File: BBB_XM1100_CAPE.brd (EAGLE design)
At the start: 54.6 x 71.8 mm, 24 parts, among them U2 MIC5225-3.3

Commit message: BOM updates associated with populating first test boards
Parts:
- C4: value 1uF -> 47pF
- L1: value 33NH -> 39NH
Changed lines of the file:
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@@
 <attribute name="NAME" x="41.021" y="20.955" size="1.27" layer="25" ratio="10" rot="R90"/>
 </element>
-<element name="C4" library="rcl" package="C0805" value="1uF" x="16.51" y="11.43" smashed="yes" rot="R180">
+<element name="C4" library="rcl" package="C0805" value="47pF" x="16.51" y="11.43" smashed="yes" rot="R180">
 <attribute name="NAME" x="16.764" y="12.954" size="0.508" layer="25" rot="R180"/>
 </element>
-<element name="L1" library="SparkFun-Coils" package="0402" value="33NH" x="20.066" y="11.176" smashed="yes" rot="R180">
+<element name="L1" library="SparkFun-Coils" package="0402" value="39NH" x="20.066" y="11.176" smashed="yes" rot="R180">
 <attribute name="NAME" x="20.447" y="12.446" size="0.508" layer="25" rot="R180"/>
 <attribute name="PROD_ID" value="NDUC-13457" x="20.066" y="11.176" size="1.778" layer="27" rot="R180" display="off"/>

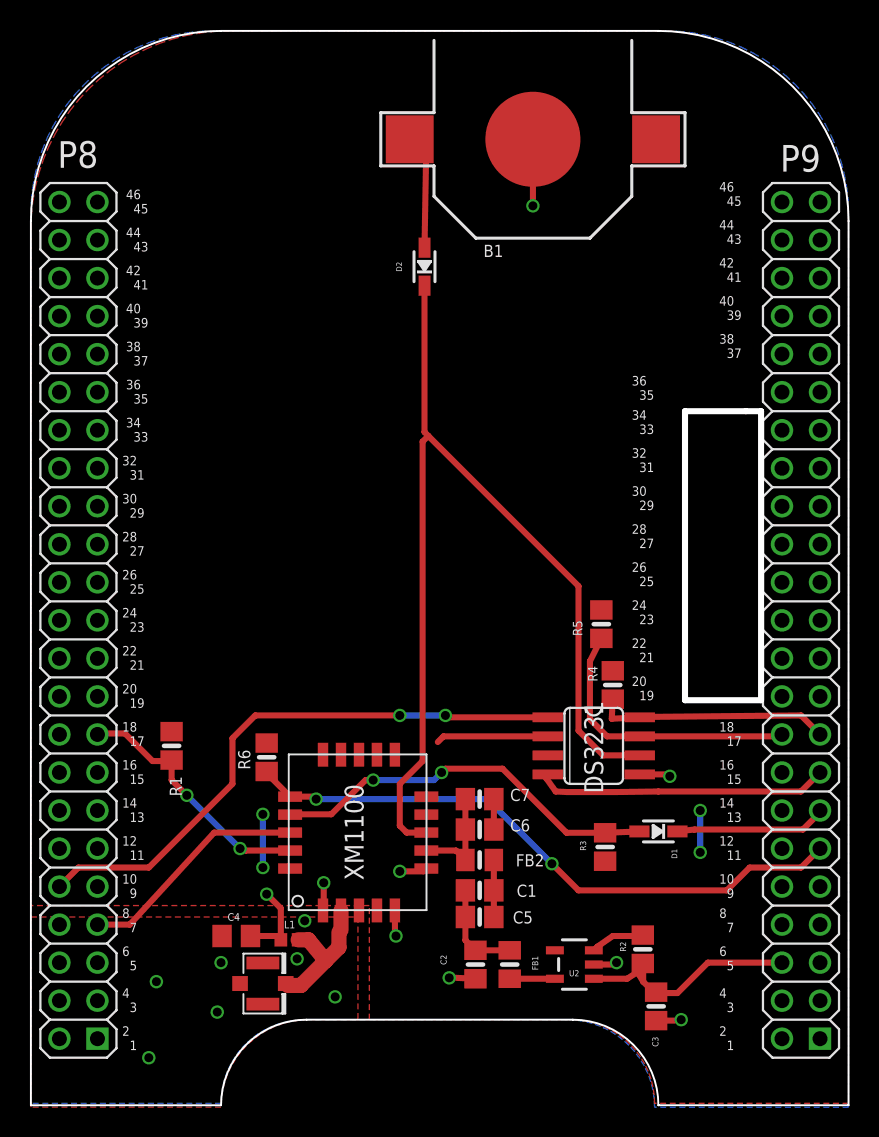
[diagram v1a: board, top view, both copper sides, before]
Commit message: minor updates to silkscreen layout to better match OSH Park silkscreen resolution
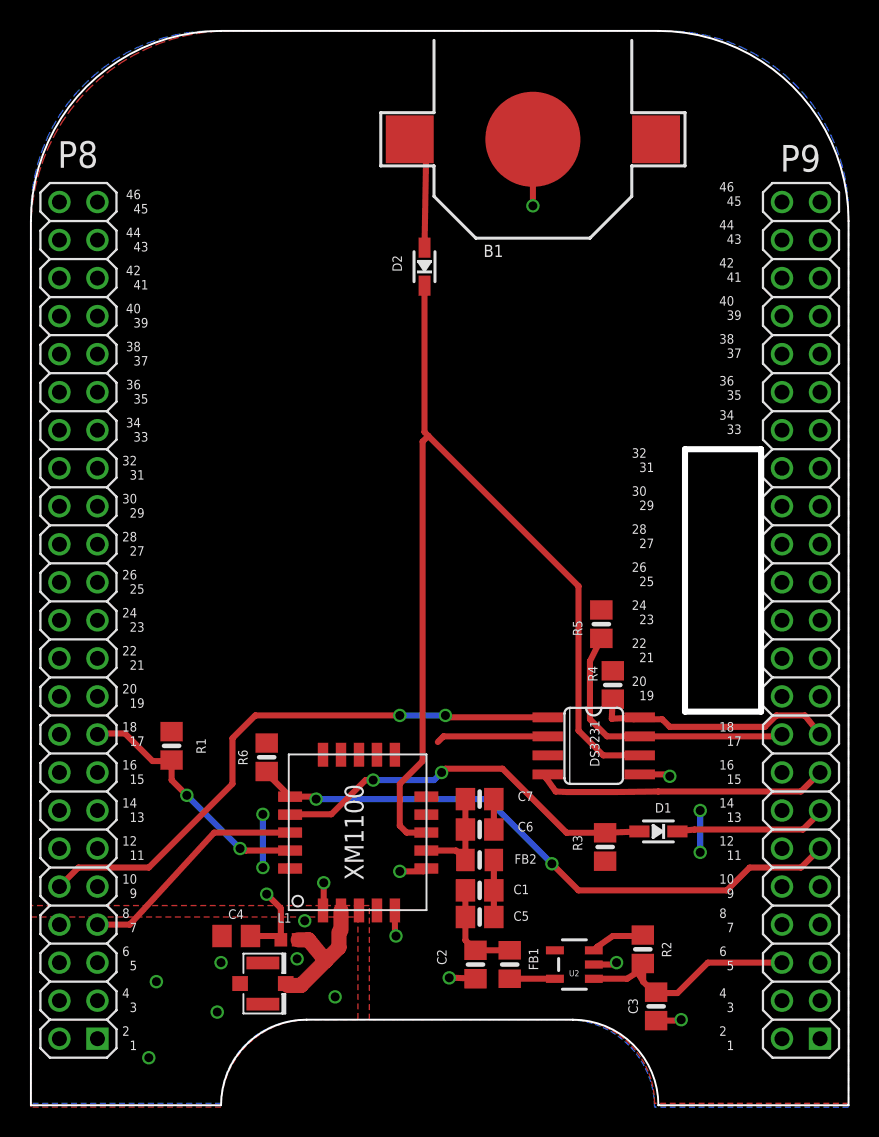
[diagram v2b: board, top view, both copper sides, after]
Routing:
- net SCL: track 15.7 -> 17.2 mm
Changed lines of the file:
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@@
 <text x="4.572" y="62.738" size="1.778" layer="25">P8</text>
 <polygon width="0.4064" layer="20">
-<vertex x="50.546" y="46.482"/>
-<vertex x="46.482" y="46.482"/>
-<vertex x="46.482" y="27.178"/>
-<vertex x="51.562" y="27.178"/>
-<vertex x="51.562" y="46.482"/>
+<vertex x="51.562" y="43.942"/>
+<vertex x="46.482" y="43.942"/>
+<vertex x="46.482" y="26.416"/>
+<vertex x="51.562" y="26.416"/>
 </polygon>
 <text x="8.89" y="3.81" size="0.635" layer="25">2
@@
 <text x="48.768" y="50.038" size="0.635" layer="25">38
   37</text>
-<text x="42.926" y="47.244" size="0.635" layer="25">36
+<text x="48.768" y="47.244" size="0.635" layer="25">36
   35</text>
-<text x="42.926" y="44.958" size="0.635" layer="25">34
+<text x="48.768" y="44.958" size="0.635" layer="25">34
   33</text>
 <text x="42.926" y="42.418" size="0.635" layer="25">32
@@
 </element>
 <element name="R2" library="microbuilder" package="0805-NO" value="10K" x="43.664" y="10.541" smashed="yes" rot="R270">
-<attribute name="NAME" x="42.14" y="11.049" size="0.4064" layer="25" ratio="15" rot="R270"/>
+<attribute name="NAME" x="44.934" y="11.049" size="0.635" layer="25" rot="R270"/>
 </element>
 <element name="C2" library="microbuilder" package="0805-NO" value="10uF" x="32.488" y="9.525" smashed="yes" rot="R270">
-<attribute name="NAME" x="30.559" y="9.501" size="0.4064" layer="25" ratio="15" rot="R90"/>
+<attribute name="NAME" x="30.559" y="9.501" size="0.635" layer="25" rot="R90"/>
 </element>
 <element name="FB1" library="microbuilder" package="0805-NO@1" value="Ferrite" x="34.774" y="9.525" smashed="yes" rot="R90">
-<attribute name="NAME" x="36.679" y="9.144" size="0.4064" layer="25" ratio="15" rot="R90"/>
+<attribute name="NAME" x="36.679" y="9.144" size="0.635" layer="25" rot="R90"/>
 </element>
 <element name="C3" library="microbuilder" package="0805-NO" value="10uF" x="44.553" y="6.731" smashed="yes" rot="R270">
-<attribute name="NAME" x="44.299" y="4.699" size="0.4064" layer="25" ratio="15" rot="R270"/>
+<attribute name="NAME" x="43.331" y="6.223" size="0.635" layer="25" rot="R90"/>
 </element>
 <element name="D1" library="microbuilder" package="SOD-323" value="1N4148" x="44.704" y="18.415" smashed="yes" rot="R180">
-<attribute name="NAME" x="45.582" y="17.25" size="0.381" layer="25" font="vector" ratio="15" rot="R270"/>
+<attribute name="NAME" x="44.472" y="19.674" size="0.635" layer="25" font="vector"/>
 </element>
 <element name="R3" library="microbuilder" package="0805-NO" value="10K" x="41.148" y="17.375" smashed="yes" rot="R90">
-<attribute name="NAME" x="39.878" y="17.121" size="0.4064" layer="25" ratio="15" rot="R90"/>
-</element>
-<element name="B1" library="microbuilder" package="CR1220" value="CR1220" x="36.322" y="64.643"/>
+<attribute name="NAME" x="39.624" y="17.121" size="0.635" layer="25" rot="R90"/>
+</element>
+<element name="B1" library="microbuilder" package="CR1220" value="CR1220" x="36.322" y="64.643" smashed="yes">
+<attribute name="NAME" x="33.02" y="56.783" size="0.8128" layer="25" font="vector" ratio="18"/>
+<attribute name="VALUE" x="33.02" y="55.775" size="0.635" layer="27" font="vector"/>
+</element>
 <element name="U$20" library="microbuilder" package="U.FL" value="U.FL" x="18.288" y="8.255" smashed="yes"/>
 <element name="D2" library="microbuilder" package="SOD-323" value="CUS520" x="29.083" y="56.134" smashed="yes" rot="R90">
-<attribute name="NAME" x="27.575" y="55.796" size="0.381" layer="25" ratio="18" rot="R90"/>
+<attribute name="NAME" x="27.575" y="55.796" size="0.635" layer="25" rot="R90"/>
 </element>
 <element name="U$15" library="adafruit" package="BEAGLEBONE_SHIELD" value="BEAGLEBONE_OUTLINE" x="2.794" y="-14.478" smashed="yes"/>
 <element name="R4" library="microbuilder" package="0805-NO" value="10K" x="41.656" y="28.194" smashed="yes" rot="R270">
-<attribute name="NAME" x="40.005" y="29.464" size="0.635" layer="25" ratio="18" rot="R270"/>
+<attribute name="NAME" x="40.005" y="29.464" size="0.635" layer="25" rot="R270"/>
 </element>
 <element name="R5" library="microbuilder" package="0805-NO" value="10K" x="40.894" y="32.258" smashed="yes" rot="R270">
-<attribute name="NAME" x="38.989" y="32.512" size="0.635" layer="25" ratio="18" rot="R270"/>
+<attribute name="NAME" x="38.989" y="32.512" size="0.635" layer="25" rot="R270"/>
 </element>
 <element name="DS3231" library="tuckerLib" package="SO08" value="DS3231M-8PIN" x="40.386" y="24.13" smashed="yes" rot="R270">
-<attribute name="NAME" x="41.021" y="20.955" size="1.27" layer="25" ratio="10" rot="R90"/>
+<attribute name="NAME" x="40.767" y="22.733" size="0.635" layer="25" rot="R90"/>
 </element>
 <element name="C4" library="rcl" package="C0805" value="47pF" x="16.51" y="11.43" smashed="yes" rot="R180">
-<attribute name="NAME" x="16.764" y="12.954" size="0.508" layer="25" rot="R180"/>
+<attribute name="NAME" x="17.018" y="13.208" size="0.635" layer="25" rot="R180"/>
 </element>
 <element name="L1" library="SparkFun-Coils" package="0402" value="39NH" x="20.066" y="11.176" smashed="yes" rot="R180">
-<attribute name="NAME" x="20.447" y="12.446" size="0.508" layer="25" rot="R180"/>
+<attribute name="NAME" x="20.193" y="12.954" size="0.635" layer="25" rot="R180"/>
 <attribute name="PROD_ID" value="NDUC-13457" x="20.066" y="11.176" size="1.778" layer="27" rot="R180" display="off"/>
 <attribute name="VALUE" value="3.9NH" x="20.066" y="11.176" size="1.778" layer="27" rot="R180" display="off"/>
@@
 <element name="U$3" library="tuckerLib" package="XM1100" value="XM1100" x="26.416" y="19.558" smashed="yes" rot="R90"/>
 <element name="FB2" library="microbuilder" package="0805-NO@1" value="Ferrite" x="32.766" y="16.51" smashed="yes" rot="R180">
-<attribute name="NAME" x="37.084" y="16.891" size="0.8128" layer="25" ratio="18" rot="R180"/>
+<attribute name="NAME" x="36.576" y="16.891" size="0.635" layer="25" rot="R180"/>
 </element>
 <element name="C1" library="microbuilder" package="0805-NO" value="1.0uF" x="32.766" y="14.478" smashed="yes" rot="R180">
-<attribute name="NAME" x="36.576" y="14.859" size="0.8128" layer="25" ratio="18" rot="R180"/>
+<attribute name="NAME" x="36.068" y="14.859" size="0.635" layer="25" rot="R180"/>
 </element>
 <element name="C5" library="microbuilder" package="0805-NO" value="0.1uF" x="32.766" y="12.7" smashed="yes" rot="R180">
-<attribute name="NAME" x="36.322" y="13.081" size="0.8128" layer="25" ratio="18" rot="R180"/>
+<attribute name="NAME" x="36.068" y="13.081" size="0.635" layer="25" rot="R180"/>
 </element>
 <element name="C6" library="microbuilder" package="0805-NO" value="1.0uF" x="32.766" y="18.542" smashed="yes">
-<attribute name="NAME" x="34.798" y="18.415" size="0.8128" layer="25" ratio="18"/>
+<attribute name="NAME" x="35.306" y="18.415" size="0.635" layer="25"/>
 </element>
 <element name="C7" library="microbuilder" package="0805-NO" value="0.1uF" x="32.766" y="20.574" smashed="yes">
-<attribute name="NAME" x="34.798" y="20.447" size="0.8128" layer="25" ratio="18"/>
+<attribute name="NAME" x="35.306" y="20.447" size="0.635" layer="25"/>
 </element>
 <element name="R1" library="microbuilder" package="0805-NO" value="10K" x="12.192" y="24.13" smashed="yes" rot="R270">
-<attribute name="NAME" x="12.065" y="22.098" size="0.8128" layer="25" ratio="18" rot="R270"/>
+<attribute name="NAME" x="13.843" y="24.638" size="0.635" layer="25" rot="R270"/>
 </element>
 <element name="R6" library="microbuilder" package="0805-NO" value="10K" x="18.542" y="23.368" smashed="yes" rot="R270">
-<attribute name="NAME" x="16.637" y="23.876" size="0.8128" layer="25" ratio="18" rot="R270"/>
+<attribute name="NAME" x="16.637" y="23.876" size="0.635" layer="25" rot="R270"/>
 </element>
 </elements>
@@
 <contactref element="U$15" pad="63"/>
 <wire x1="41.656" y1="27.244" x2="41.59" y2="25.941" width="0.4064" layer="1"/>
-<wire x1="41.59" y1="25.941" x2="43.4594" y2="26.035" width="0.4064" layer="1"/>
-<wire x1="54.229" y1="26.162" x2="55.499" y2="24.892" width="0.4064" layer="1"/>
-<wire x1="54.229" y1="26.162" x2="43.688" y2="26.0604" width="0.4064" layer="1"/>
+<wire x1="41.59" y1="25.941" x2="42.920975" y2="26.007925" width="0.4064" layer="1"/>
+<wire x1="42.920975" y1="26.007925" x2="43.4594" y2="26.035" width="0.4064" layer="1"/>
+<wire x1="54.483" y1="26.162" x2="55.499" y2="24.892" width="0.4064" layer="1"/>
 <wire x1="43.688" y1="26.0604" x2="43.4594" y2="26.035" width="0.4064" layer="1"/>
+<wire x1="54.483" y1="26.162" x2="52.578" y2="26.162" width="0.4064" layer="1"/>
+<wire x1="52.578" y1="26.162" x2="51.816" y2="25.4" width="0.4064" layer="1"/>
+<wire x1="51.816" y1="25.4" x2="45.466" y2="25.4" width="0.4064" layer="1"/>
+<wire x1="45.466" y1="25.4" x2="44.958" y2="25.908" width="0.4064" layer="1"/>
+<wire x1="44.958" y1="25.908" x2="43.0209" y2="25.908" width="0.4064" layer="1"/>
+<wire x1="43.0209" y1="25.908" x2="42.920975" y2="26.007925" width="0.4064" layer="1"/>
 </signal>
 <signal name="SQW">
